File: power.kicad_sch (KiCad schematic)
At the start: 22 parts, among them U1 LM317_SOT-223, U2 NE5532, U3 NE5532

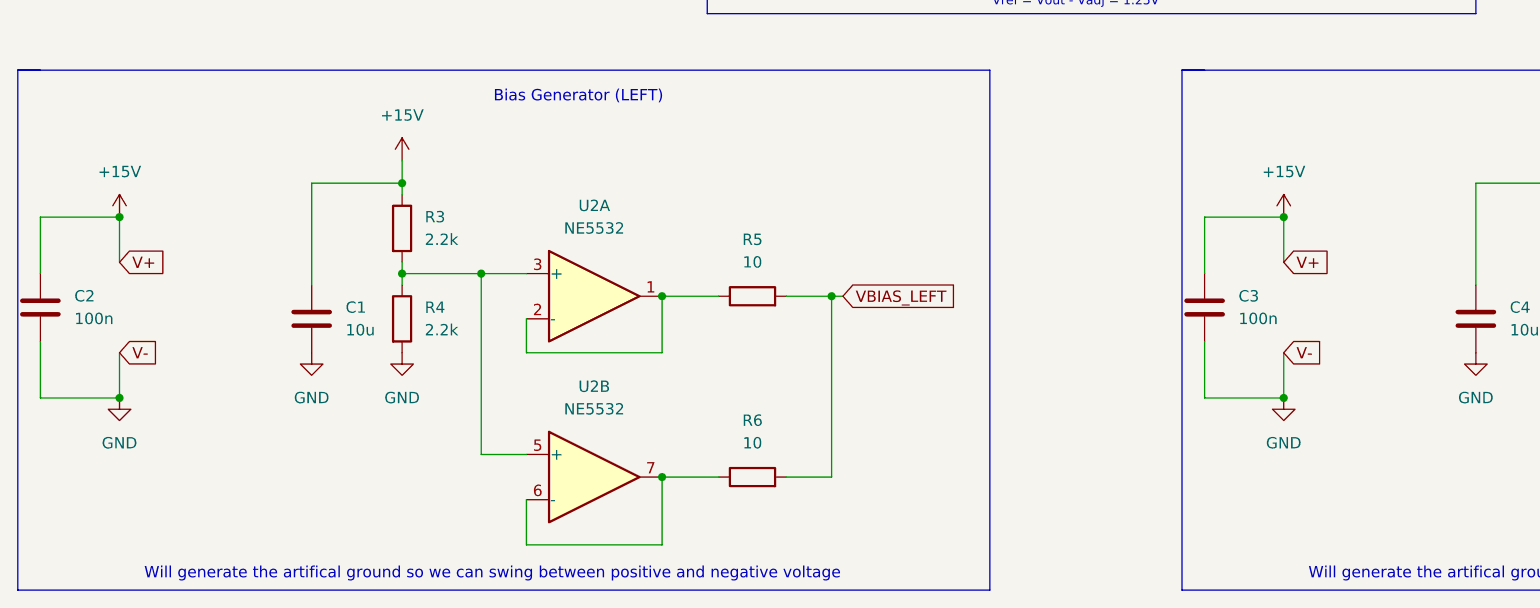
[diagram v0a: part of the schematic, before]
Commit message: Finish Input Buffer & Add Volume Control Sheet
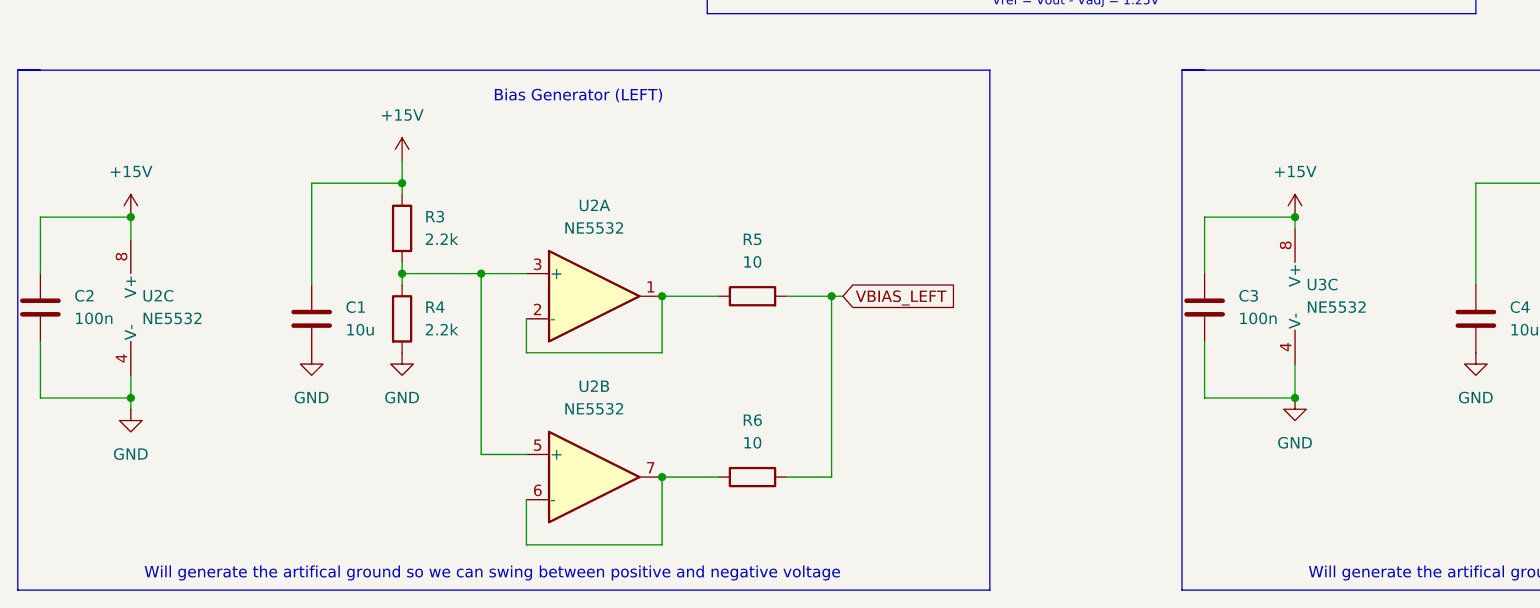
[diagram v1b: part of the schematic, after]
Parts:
- added unit 3 of U2
- added unit 3 of U3
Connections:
- net +15V: now also U2.8 (V+), U3.8 (V+)
- net GND: now also U2.4 (V-), U3.4 (V-)

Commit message: Add Footprints
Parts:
- C1, C2, C3, C4: footprint (none) -> Capacitor_SMD:C_0805_2012Metric
- CAdjust1: renamed from CAdjust; footprint (none) -> Capacitor_SMD:CP_Elec_5x5.3
- Ci1: renamed from Ci; footprint (none) -> Capacitor_SMD:CP_Elec_5x5.3
- Co1: renamed from Co; footprint (none) -> Capacitor_SMD:CP_Elec_5x5.3
- R1, R10, R2, R3, R4, R5, R6, R7, R8, R9: footprint (none) -> Resistor_SMD:R_0805_2012Metric
- U2, U3: footprint (none) -> Package_SO:SOIC-8_3.9x4.9mm_P1.27mm
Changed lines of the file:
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@@
 			)
 		)
-		(property "Footprint" ""
+		(property "Footprint" "Resistor_SMD:R_0805_2012Metric"
 			(at 110.49 131.318 90)
 			(effects
@@
 			)
 		)
-		(property "Footprint" ""
+		(property "Footprint" "Capacitor_SMD:C_0805_2012Metric"
 			(at 162.2552 114.3 0)
 			(effects
@@
 			)
 		)
-		(property "Footprint" ""
+		(property "Footprint" "Capacitor_SMD:C_0805_2012Metric"
 			(at 31.4452 114.3 0)
 			(effects
@@
 			)
 		)
-		(property "Footprint" ""
+		(property "Footprint" "Capacitor_SMD:C_0805_2012Metric"
 			(at 192.7352 115.57 0)
 			(effects
@@
 			)
 		)
-		(property "Footprint" ""
+		(property "Footprint" "Resistor_SMD:R_0805_2012Metric"
 			(at 110.49 110.998 90)
 			(effects
@@
 			)
 		)
-		(property "Footprint" ""
+		(property "Footprint" "Resistor_SMD:R_0805_2012Metric"
 			(at 134.112 58.42 90)
 			(effects
@@
 			)
 		)
-		(property "Footprint" ""
+		(property "Footprint" "Package_SO:SOIC-8_3.9x4.9mm_P1.27mm"
 			(at 43.18 110.49 0)
 			(effects
@@
 			)
 		)
-		(property "Footprint" ""
+		(property "Footprint" "Package_SO:SOIC-8_3.9x4.9mm_P1.27mm"
 			(at 173.99 109.22 0)
 			(effects
@@
 			)
 		)
-		(property "Footprint" ""
+		(property "Footprint" "Package_SO:SOIC-8_3.9x4.9mm_P1.27mm"
 			(at 223.52 109.22 0)
 			(effects
@@
 			)
 		)
-		(property "Footprint" ""
+		(property "Footprint" "Resistor_SMD:R_0805_2012Metric"
 			(at 69.342 101.6 90)
 			(effects
@@
 		(dnp no)
 		(fields_autoplaced yes)
-		(property "Reference" "CAdjust"
+		(property "Reference" "CAdjust1"
 			(at 160.02 56.2609 0)
 			(effects
@@
 			)
 		)
-		(property "Footprint" ""
+		(property "Footprint" "Capacitor_SMD:CP_Elec_5x5.3"
 			(at 157.1752 62.23 0)
 			(effects
@@
 			(project "Amp"
 				(path "/5faae81d-f66a-438b-a97a-07010798add6/97cb9c44-c831-444c-aa77-3756bc34400e"
-					(reference "CAdjust")
+					(reference "CAdjust1")
 					(unit 1)
 				)
@@
 			)
 		)
-		(property "Footprint" ""
+		(property "Footprint" "Package_SO:SOIC-8_3.9x4.9mm_P1.27mm"
 			(at 223.52 129.54 0)
 			(effects
@@
 			)
 		)
-		(property "Footprint" ""
+		(property "Footprint" "Resistor_SMD:R_0805_2012Metric"
 			(at 200.152 101.6 90)
 			(effects
@@
 			)
 		)
-		(property "Footprint" ""
+		(property "Footprint" "Resistor_SMD:R_0805_2012Metric"
 			(at 241.3 131.318 90)
 			(effects
@@
 			)
 		)
-		(property "Footprint" ""
+		(property "Footprint" "Capacitor_SMD:C_0805_2012Metric"
 			(at 61.9252 115.57 0)
 			(effects
@@
 			)
 		)
-		(property "Footprint" ""
+		(property "Footprint" "Resistor_SMD:R_0805_2012Metric"
 			(at 241.3 110.998 90)
 			(effects
@@
 		(dnp no)
 		(fields_autoplaced yes)
-		(property "Reference" "Co"
+		(property "Reference" "Co1"
 			(at 175.26 51.1809 0)
 			(effects
@@
 			)
 		)
-		(property "Footprint" ""
+		(property "Footprint" "Capacitor_SMD:CP_Elec_5x5.3"
 			(at 172.4152 57.15 0)
 			(effects
@@
 			(project "Amp"
 				(path "/5faae81d-f66a-438b-a97a-07010798add6/97cb9c44-c831-444c-aa77-3756bc34400e"
-					(reference "Co")
+					(reference "Co1")
 					(unit 1)
 				)
@@
 			)
 		)
-		(property "Footprint" ""
+		(property "Footprint" "Resistor_SMD:R_0805_2012Metric"
 			(at 69.342 111.76 90)
 			(effects
@@
 			)
 		)
-		(property "Footprint" ""
+		(property "Footprint" "Resistor_SMD:R_0805_2012Metric"
 			(at 145.542 46.99 90)
 			(effects
@@
 		(dnp no)
 		(fields_autoplaced yes)
-		(property "Reference" "Ci"
+		(property "Reference" "Ci1"
 			(at 123.19 51.1809 0)
 			(effects
@@
 			)
 		)
-		(property "Footprint" ""
+		(property "Footprint" "Capacitor_SMD:CP_Elec_5x5.3"
 			(at 120.3452 57.15 0)
 			(effects
@@
 			(project "Amp"
 				(path "/5faae81d-f66a-438b-a97a-07010798add6/97cb9c44-c831-444c-aa77-3756bc34400e"
-					(reference "Ci")
+					(reference "Ci1")
 					(unit 1)
 				)
@@
 			)
 		)
-		(property "Footprint" ""
+		(property "Footprint" "Package_SO:SOIC-8_3.9x4.9mm_P1.27mm"
 			(at 92.71 129.54 0)
 			(effects
@@
 			)
 		)
-		(property "Footprint" ""
+		(property "Footprint" "Package_SO:SOIC-8_3.9x4.9mm_P1.27mm"
 			(at 92.71 109.22 0)
 			(effects
@@
 			)
 		)
-		(property "Footprint" ""
+		(property "Footprint" "Resistor_SMD:R_0805_2012Metric"
 			(at 200.152 111.76 90)
 			(effects

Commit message: Add inputs audio and power and correct errors
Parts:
- added J4: Barrel_Jack, Connector_BarrelJack:BarrelJack_Horizontal, symbol Connector:Barrel_Jack
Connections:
- net Vo is gone; now on net +15V: Co1.1, D1.2 (A), D2.1 (K), R1.1, U1.2 (VO)
- net GND: now also J4.2
- net Vi: now also J4.1
